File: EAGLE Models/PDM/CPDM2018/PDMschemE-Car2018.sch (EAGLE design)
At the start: 42 parts, among them Q1 2N2907, Q2 2N2907, Q3 2N2907, Q4 2N2907, Q5 2N2907, Q6 2N2907

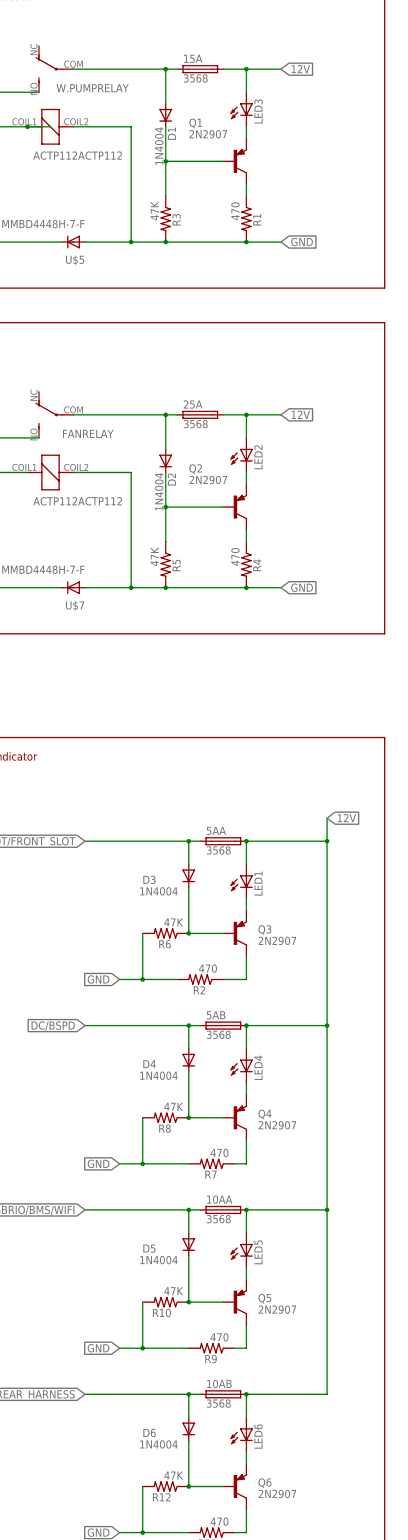
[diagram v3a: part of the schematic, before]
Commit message: Spec'd component on schem.
All components should be properly spec'd and are avaiable through digikey. LED's are currently all red, subject to change but will require adjusting certain resistant values (little work).
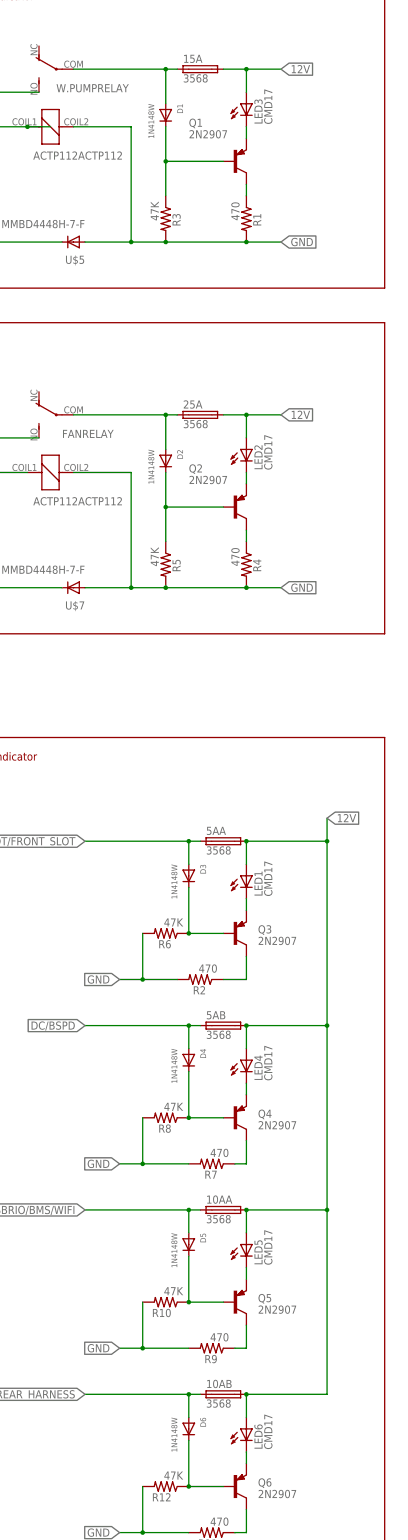
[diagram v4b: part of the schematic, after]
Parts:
- D1, D2, D3, D4, D5, D6: value 1N4004 -> 1N4148W; device adafruit:1N4004 -> adafruit:DIODESOD-123
- LED1, LED2, LED3, LED4, LED5, LED6: value (none) -> CMD17

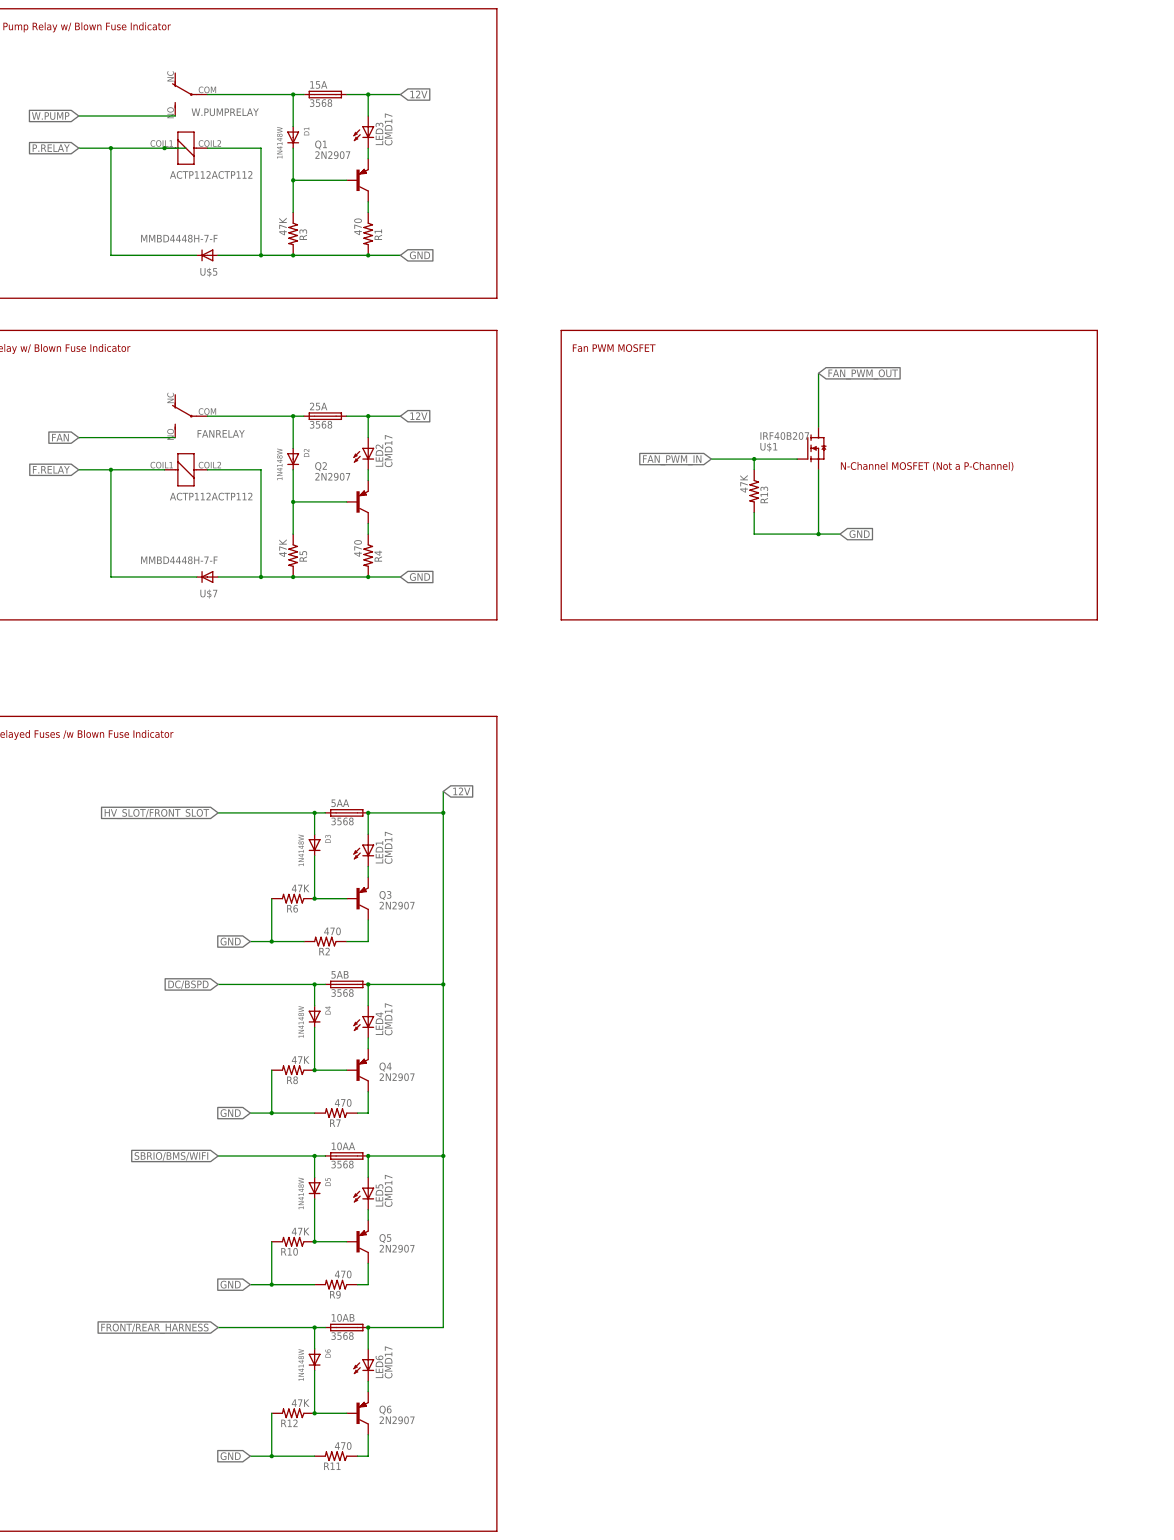
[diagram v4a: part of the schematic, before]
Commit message: finished schematic and readied board for layout
added connectors to the board where they need to be. Board is ready to be layed out
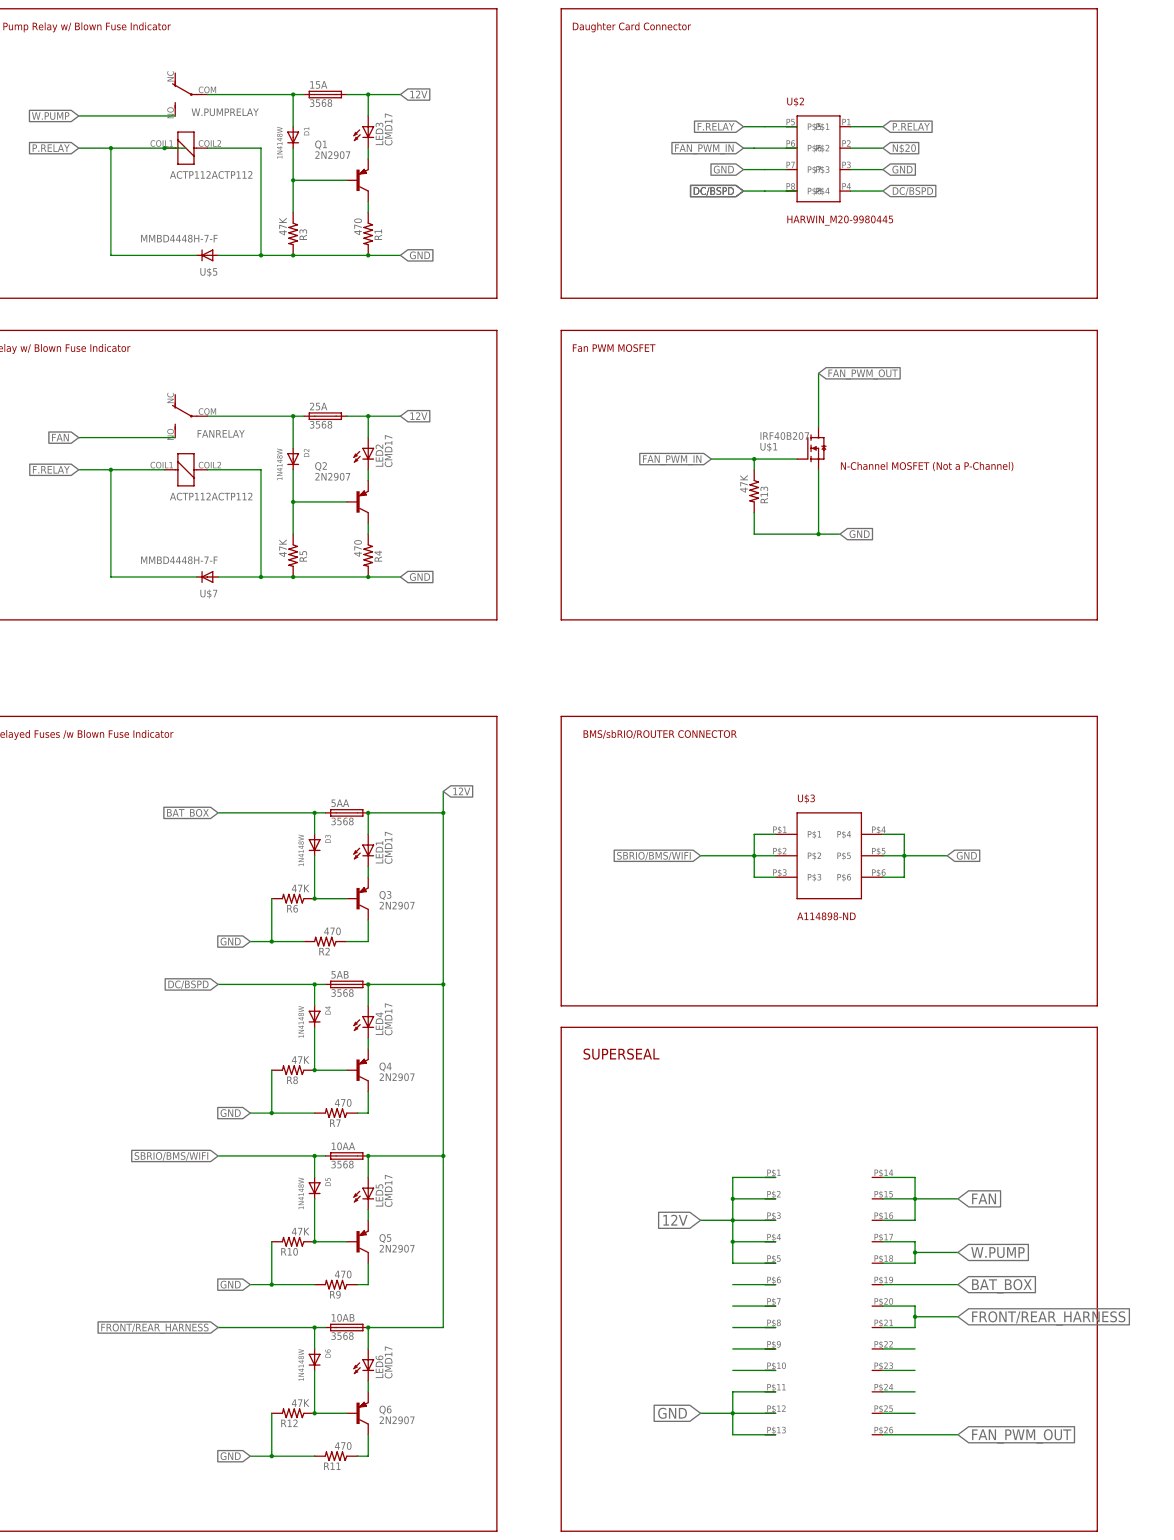
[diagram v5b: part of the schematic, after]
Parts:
- added U$2: HARWIN_M20-9980445, formula electric:HARWIN_M20-9980445
- added U$3: A114898-ND, formula electric:A114898-ND
- added U$4: SUPERSEAL1.0_26POS_2ROW, TE:SUPERSEAL1.0_26POS_2ROW
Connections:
- removed net HV_SLOT/FRONT_SLOT: 5AA.1, D3.A
- new net BAT_BOX: 5AA.1, D3.A, U$4.B19
- new net N$20: U$2.P$2
- new net N$21: U$4.B6
- new net N$25: U$4.B7
- new net N$26: U$4.B8
- new net N$30: U$4.B9
- new net N$31: U$4.B10
- new net N$43: U$4.B22
- new net N$44: U$4.B23
- new net N$45: U$4.B24
- new net N$46: U$4.B25
- net 12V: now also U$4.B1, U$4.B2, U$4.B3, U$4.B4, U$4.B5
- net DC/BSPD: now also U$2.P$4, U$2.P$8
- net F.RELAY: now also U$2.P$5
- net FAN: now also U$4.B14, U$4.B15, U$4.B16
- net FAN_PWM_IN: now also U$2.P$6
- net FAN_PWM_OUT: now also U$4.B26
- net FRONT/REAR_HARNESS: now also U$4.B20, U$4.B21
- net GND: now also U$2.P$3, U$2.P$7, U$3.P$4, U$3.P$5, U$3.P$6, U$4.B11, U$4.B12, U$4.B13
- net P.RELAY: now also U$2.P$1
- net SBRIO/BMS/WIFI: now also U$3.P$1, U$3.P$2, U$3.P$3
- net W.PUMP: now also U$4.B17, U$4.B18
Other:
- note added: "BMS/sbRIO/ROUTER CONNECTOR"
- note added: "Daughter Card Connector"
- note added: "SUPERSEAL"

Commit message: Updated board with pinout for mcu power switch
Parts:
- removed U$3: A114898-ND, formula electric:A114898-ND
- added U$6: A30605-ND, formula electric:A30605-ND
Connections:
- removed net N$43: U$4.B22
- new net MCU_POWER: U$4.B22, U$6.P$4
- net FRONT/REAR_HARNESS: now also U$6.P$8
- net GND: now also U$6.P$1, U$6.P$2, U$6.P$3; no longer U$3.P$4, U$3.P$5, U$3.P$6
- net SBRIO/BMS/WIFI: now also U$6.P$5, U$6.P$6, U$6.P$7; no longer U$3.P$1, U$3.P$2, U$3.P$3
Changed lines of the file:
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@@
 <part name="R13" library="resistor" library_urn="urn:adsk.eagle:library:348" deviceset="R-US_" device="R1206" package3d_urn="urn:adsk.eagle:package:26062/1" value="47K"/>
 <part name="U$2" library="formula electric" deviceset="HARWIN_M20-9980445" device=""/>
-<part name="U$3" library="formula electric" deviceset="A114898-ND" device=""/>
 <part name="U$4" library="TE" deviceset="SUPERSEAL1.0_26POS_2ROW" device=""/>
+<part name="U$6" library="formula electric" deviceset="A30605-ND" device=""/>
 </parts>
 <sheets>
@@
 </instance>
 <instance part="U$2" gate="G$1" x="134.62" y="228.6"/>
-<instance part="U$3" gate="G$1" x="137.16" y="63.5"/>
 <instance part="U$4" gate="G$1" x="139.7" y="-53.34"/>
+<instance part="U$6" gate="G$1" x="137.16" y="60.96"/>
 </instances>
 <busses>
@@
 </segment>
 <segment>
-<pinref part="U$3" gate="G$1" pin="P$4"/>
 <wire x1="149.86" y1="68.58" x2="154.94" y2="68.58" width="0.1524" layer="91"/>
 <wire x1="154.94" y1="68.58" x2="154.94" y2="63.5" width="0.1524" layer="91"/>
-<pinref part="U$3" gate="G$1" pin="P$6"/>
 <wire x1="154.94" y1="63.5" x2="154.94" y2="58.42" width="0.1524" layer="91"/>
-<wire x1="154.94" y1="58.42" x2="149.86" y2="58.42" width="0.1524" layer="91"/>
-<pinref part="U$3" gate="G$1" pin="P$5"/>
+<wire x1="154.94" y1="58.42" x2="152.4" y2="58.42" width="0.1524" layer="91"/>
 <wire x1="149.86" y1="63.5" x2="154.94" y2="63.5" width="0.1524" layer="91"/>
 <wire x1="165.1" y1="63.5" x2="154.94" y2="63.5" width="0.1524" layer="91"/>
 <junction x="154.94" y="63.5"/>
 <label x="165.1" y="63.5" size="1.778" layer="95" xref="yes"/>
+<pinref part="U$6" gate="G$1" pin="P$1"/>
+<pinref part="U$6" gate="G$1" pin="P$2"/>
+<pinref part="U$6" gate="G$1" pin="P$3"/>
+<wire x1="152.4" y1="58.42" x2="149.86" y2="58.42" width="0.1524" layer="91"/>
 </segment>
 <segment>
@@
 </segment>
 <segment>
-<pinref part="U$3" gate="G$1" pin="P$1"/>
 <wire x1="124.46" y1="68.58" x2="119.38" y2="68.58" width="0.1524" layer="91"/>
-<pinref part="U$3" gate="G$1" pin="P$3"/>
 <wire x1="119.38" y1="68.58" x2="119.38" y2="63.5" width="0.1524" layer="91"/>
 <wire x1="119.38" y1="63.5" x2="119.38" y2="58.42" width="0.1524" layer="91"/>
 <wire x1="119.38" y1="58.42" x2="124.46" y2="58.42" width="0.1524" layer="91"/>
-<pinref part="U$3" gate="G$1" pin="P$2"/>
 <wire x1="124.46" y1="63.5" x2="119.38" y2="63.5" width="0.1524" layer="91"/>
 <junction x="119.38" y="63.5"/>
 <wire x1="119.38" y1="63.5" x2="106.68" y2="63.5" width="0.1524" layer="91"/>
 <label x="106.68" y="63.5" size="1.778" layer="95" rot="R180" xref="yes"/>
+<pinref part="U$6" gate="G$1" pin="P$5"/>
+<pinref part="U$6" gate="G$1" pin="P$6"/>
+<pinref part="U$6" gate="G$1" pin="P$7"/>
 </segment>
 </net>
@@
 <label x="167.64" y="-45.72" size="2.54" layer="95" xref="yes"/>
 </segment>
+<segment>
+<pinref part="U$6" gate="G$1" pin="P$8"/>
+<wire x1="124.46" y1="53.34" x2="119.38" y2="53.34" width="0.1524" layer="91"/>
+<label x="119.38" y="53.34" size="1.778" layer="95" rot="R180" xref="yes"/>
+</segment>
 </net>
 <net name="N$1" class="0">
@@
 </segment>
 </net>
-<net name="N$43" class="0">
-<segment>
-<pinref part="U$4" gate="G$1" pin="B22"/>
-<wire x1="149.86" y1="-53.34" x2="157.48" y2="-53.34" width="0.1524" layer="91"/>
-</segment>
-</net>
 <net name="N$44" class="0">
 <segment>
@@
 </segment>
 </net>
+<net name="MCU_POWER" class="0">
+<segment>
+<pinref part="U$6" gate="G$1" pin="P$4"/>
+<wire x1="149.86" y1="53.34" x2="154.94" y2="53.34" width="0.1524" layer="91"/>
+<label x="154.94" y="53.34" size="1.778" layer="95" xref="yes"/>
+</segment>
+<segment>
+<pinref part="U$4" gate="G$1" pin="B22"/>
+<wire x1="149.86" y1="-53.34" x2="167.64" y2="-53.34" width="0.1524" layer="91"/>
+<label x="167.64" y="-53.34" size="2.54" layer="95" xref="yes"/>
+</segment>
+</net>

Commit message: Board design
set up traces for high current
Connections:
- removed net N$21: U$4.B6
- removed net N$44: U$4.B23
- removed net N$45: U$4.B24
- removed net N$46: U$4.B25
- net 12V: now also U$4.B22, U$4.B23, U$4.B24, U$4.B25; no longer U$4.B1, U$4.B2, U$4.B3, U$4.B4, U$4.B5
- net MCU_POWER: now also U$4.B6; no longer U$4.B22
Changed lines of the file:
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@@
 </segment>
 <segment>
-<pinref part="U$4" gate="G$1" pin="B1"/>
-<wire x1="124.46" y1="-12.7" x2="114.3" y2="-12.7" width="0.1524" layer="91"/>
-<pinref part="U$4" gate="G$1" pin="B2"/>
-<wire x1="124.46" y1="-17.78" x2="114.3" y2="-17.78" width="0.1524" layer="91"/>
-<wire x1="114.3" y1="-12.7" x2="114.3" y2="-17.78" width="0.1524" layer="91"/>
-<pinref part="U$4" gate="G$1" pin="B3"/>
-<wire x1="124.46" y1="-22.86" x2="114.3" y2="-22.86" width="0.1524" layer="91"/>
-<wire x1="114.3" y1="-17.78" x2="114.3" y2="-22.86" width="0.1524" layer="91"/>
-<junction x="114.3" y="-17.78"/>
-<pinref part="U$4" gate="G$1" pin="B4"/>
-<wire x1="124.46" y1="-27.94" x2="114.3" y2="-27.94" width="0.1524" layer="91"/>
-<wire x1="114.3" y1="-22.86" x2="114.3" y2="-27.94" width="0.1524" layer="91"/>
-<junction x="114.3" y="-22.86"/>
-<pinref part="U$4" gate="G$1" pin="B5"/>
-<wire x1="124.46" y1="-33.02" x2="114.3" y2="-33.02" width="0.1524" layer="91"/>
-<wire x1="114.3" y1="-27.94" x2="114.3" y2="-33.02" width="0.1524" layer="91"/>
-<junction x="114.3" y="-27.94"/>
-<wire x1="114.3" y1="-22.86" x2="106.68" y2="-22.86" width="0.1524" layer="91"/>
-<label x="106.68" y="-22.86" size="2.54" layer="95" rot="R180" xref="yes"/>
+<pinref part="U$4" gate="G$1" pin="B25"/>
+<wire x1="149.86" y1="-68.58" x2="157.48" y2="-68.58" width="0.1524" layer="91"/>
+<pinref part="U$4" gate="G$1" pin="B24"/>
+<wire x1="149.86" y1="-63.5" x2="157.48" y2="-63.5" width="0.1524" layer="91"/>
+<wire x1="157.48" y1="-68.58" x2="157.48" y2="-63.5" width="0.1524" layer="91"/>
+<pinref part="U$4" gate="G$1" pin="B23"/>
+<wire x1="149.86" y1="-58.42" x2="157.48" y2="-58.42" width="0.1524" layer="91"/>
+<wire x1="157.48" y1="-63.5" x2="157.48" y2="-60.96" width="0.1524" layer="91"/>
+<wire x1="157.48" y1="-60.96" x2="157.48" y2="-58.42" width="0.1524" layer="91"/>
+<wire x1="157.48" y1="-58.42" x2="157.48" y2="-53.34" width="0.1524" layer="91"/>
+<pinref part="U$4" gate="G$1" pin="B22"/>
+<wire x1="157.48" y1="-53.34" x2="149.86" y2="-53.34" width="0.1524" layer="91"/>
+<wire x1="167.64" y1="-60.96" x2="157.48" y2="-60.96" width="0.1524" layer="91"/>
+<junction x="157.48" y="-60.96"/>
+<junction x="157.48" y="-58.42"/>
+<junction x="157.48" y="-63.5"/>
+<label x="167.64" y="-60.96" size="1.778" layer="95" xref="yes"/>
 </segment>
 </net>
@@
 </segment>
 </net>
-<net name="N$21" class="0">
-<segment>
-<pinref part="U$4" gate="G$1" pin="B6"/>
-<wire x1="124.46" y1="-38.1" x2="114.3" y2="-38.1" width="0.1524" layer="91"/>
-</segment>
-</net>
 <net name="N$25" class="0">
 <segment>
@@
 <pinref part="U$4" gate="G$1" pin="B10"/>
 <wire x1="124.46" y1="-58.42" x2="114.3" y2="-58.42" width="0.1524" layer="91"/>
-</segment>
-</net>
-<net name="N$44" class="0">
-<segment>
-<pinref part="U$4" gate="G$1" pin="B23"/>
-<wire x1="149.86" y1="-58.42" x2="157.48" y2="-58.42" width="0.1524" layer="91"/>
-</segment>
-</net>
-<net name="N$45" class="0">
-<segment>
-<pinref part="U$4" gate="G$1" pin="B24"/>
-<wire x1="149.86" y1="-63.5" x2="157.48" y2="-63.5" width="0.1524" layer="91"/>
-</segment>
-</net>
-<net name="N$46" class="0">
-<segment>
-<pinref part="U$4" gate="G$1" pin="B25"/>
-<wire x1="149.86" y1="-68.58" x2="157.48" y2="-68.58" width="0.1524" layer="91"/>
 </segment>
 </net>
@@
 </segment>
 <segment>
-<pinref part="U$4" gate="G$1" pin="B22"/>
-<wire x1="149.86" y1="-53.34" x2="167.64" y2="-53.34" width="0.1524" layer="91"/>
-<label x="167.64" y="-53.34" size="2.54" layer="95" xref="yes"/>
-</segment>
-</net>
+<pinref part="U$4" gate="G$1" pin="B6"/>
+<wire x1="124.46" y1="-38.1" x2="106.68" y2="-38.1" width="0.1524" layer="91"/>
+<label x="106.68" y="-38.1" size="1.778" layer="95" rot="R180" xref="yes"/>
+</segment>
+</net>
